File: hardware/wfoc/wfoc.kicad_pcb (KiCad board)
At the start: 2 copper layers, 51 x 50 mm, 77 parts, among them Q1 NMOS, Q2 NMOS, Q3 NMOS, Q4 NMOS, Q5 NMOS, Q6 NMOS, U2 XOPA2333, U3 TSSOP20, U4 6209

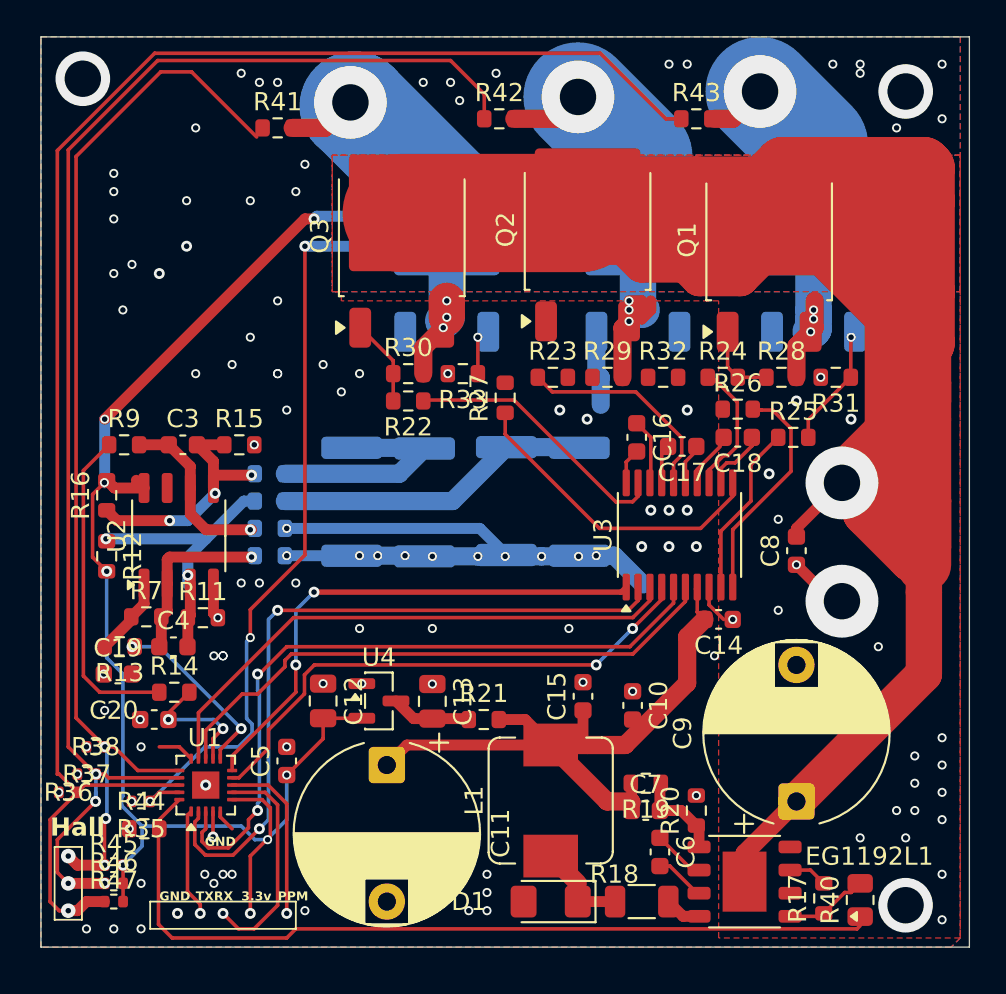
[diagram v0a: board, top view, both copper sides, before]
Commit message: 修改好了 把所有规则删掉就可以正常铺铜了
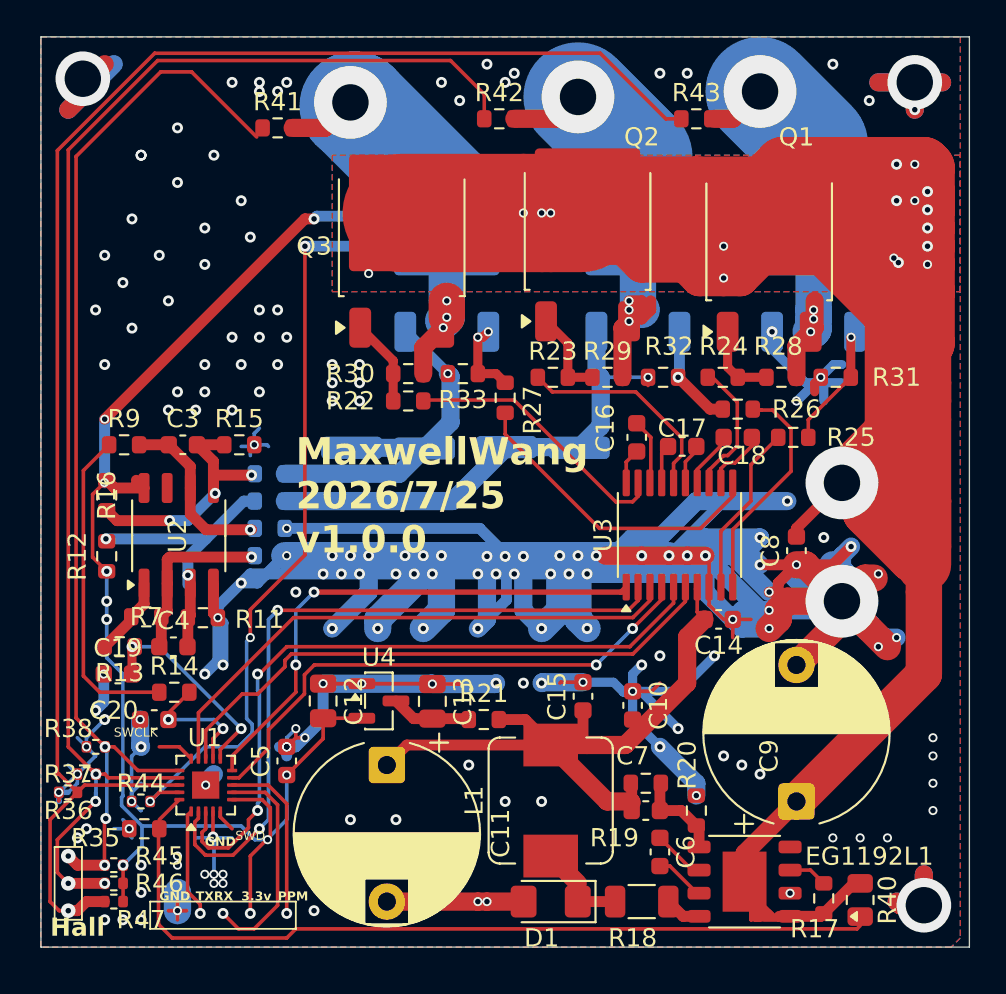
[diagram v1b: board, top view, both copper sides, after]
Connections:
- U1 pad 21: unconnected-(U1-GND-Pad21) -> Ia_N
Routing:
- net Ia_N: track 42.0 -> 381.5 mm, vias 126 -> 178
- net Ia_P: track 12.3 -> 20.3 mm
- net Ib_P: track 21.5 -> 27.4 mm, vias 0 -> 1
- net LO2: track 0.00 -> 5.50 mm, vias 0 -> 1
- net Net-(Q2-G): track 0.00 -> 4.92 mm
- net LO1: track 2.70 -> 4.40 mm, vias 1 -> 2
- net IC_ib: track 9.99 -> 11.6 mm
- net +BATT: track 194.6 -> 195.2 mm, vias 1 -> 18
- net unconnected-(U1-GND-Pad21): vias 1 -> 0
- net +3.3V: vias 8 -> 10
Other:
- board text added: "MaxwellWang 2026/7/25 v1.0.0"
- board text added: "SWCLK"
- board text added: "SWD"
